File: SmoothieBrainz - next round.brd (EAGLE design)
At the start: 101 x 101 mm, 238 parts, among them IC1 LPC1769, IC7 74LVC1G04, Q1 BSL207SP, Q2 12MHz, SW1 SW_TACT_4P_B, SW3 SW_TACT_4P_B, T1 BC817, U3 USD-SOCKETUSD, X1 MSTBA2, X14 USBPTH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

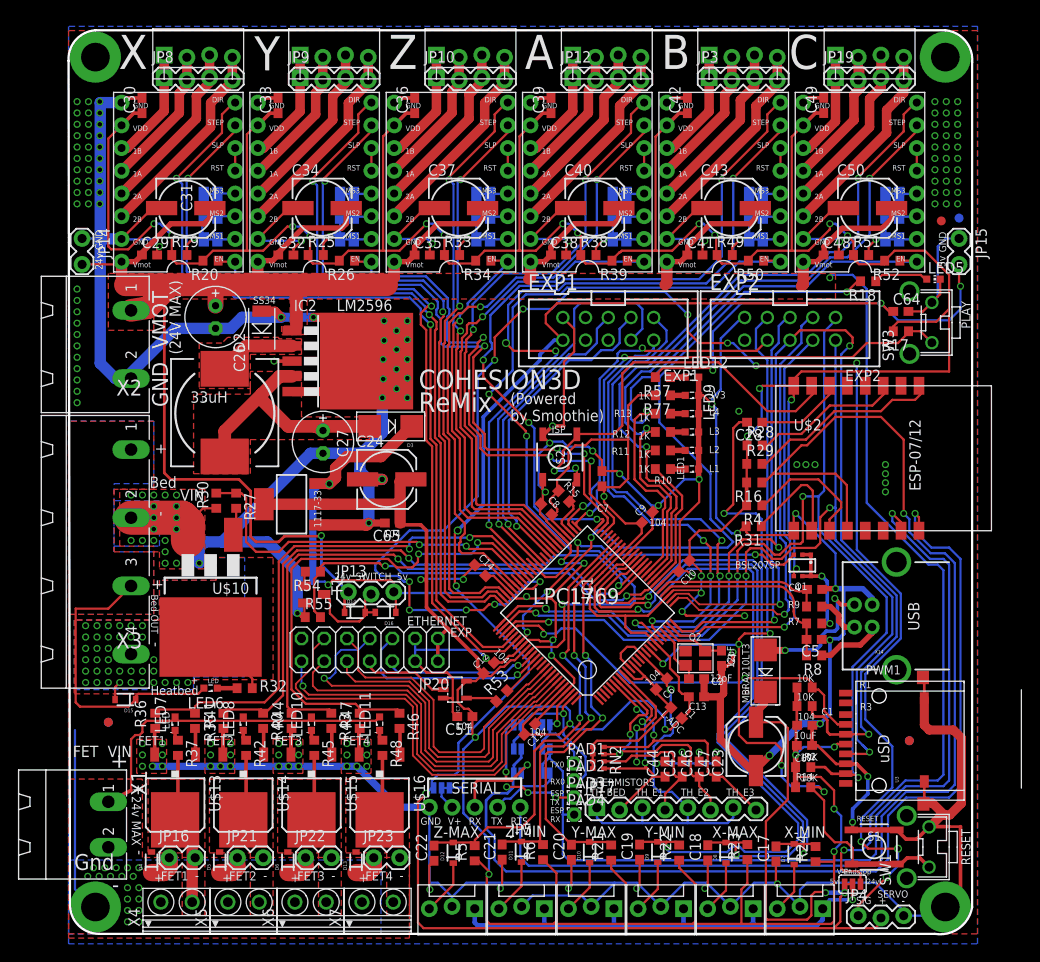
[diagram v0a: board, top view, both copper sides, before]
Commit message: Major routing cleanup per feedback from real engineer
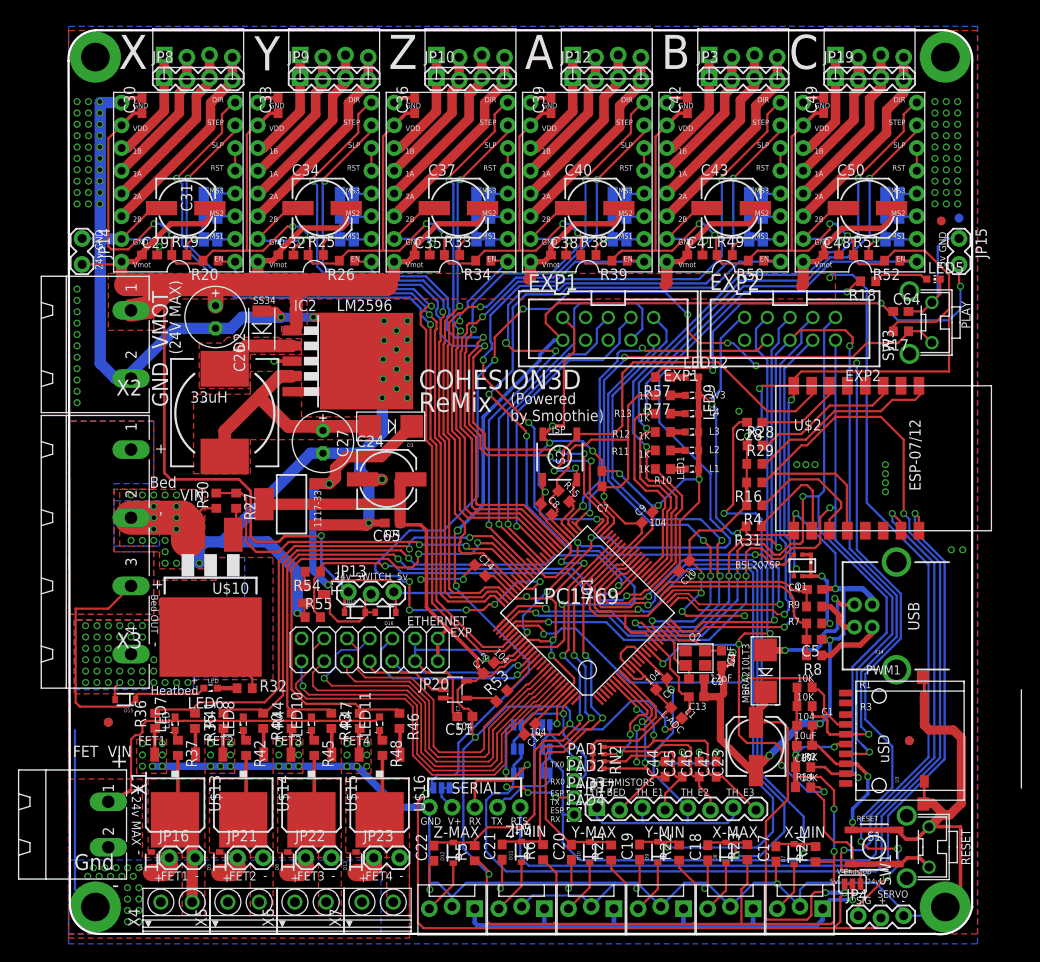
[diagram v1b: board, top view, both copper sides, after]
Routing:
- net Y_MIN: track 86.2 -> 77.3 mm
- net X_MAX: track 78.7 -> 71.8 mm
- net ESPRX: track 101.1 -> 95.6 mm
- net ESPTX: track 119.4 -> 113.9 mm
- net LED4: track 69.4 -> 64.1 mm
- net RTS: track 136.8 -> 131.8 mm
- net 24V: track 318.6 -> 314.5 mm
- net X_MIN: track 70.3 -> 66.8 mm
- net LED3: track 77.0 -> 73.6 mm
- net LED2: track 79.2 -> 76.7 mm
- net DIR1: track 95.0 -> 93.2 mm
- net STP1: track 87.4 -> 85.6 mm
- net EN2: track 58.4 -> 56.9 mm
- net BUZZER-RRD: track 59.1 -> 57.7 mm
- net P1_30_CLICK-ON-RRD: track 49.6 -> 48.2 mm
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
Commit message: About to fix ethernet
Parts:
- C1, C11, C12, C51, C6, C65: value .1uF -> 104
- D2: value (none) -> SS34
- IC2: value (none) -> LM2596-5
- LED1, LED2, LED3, LED4, LED9: value (none) -> GREEN
- LED10, LED11, LED8: value LED -> RED
- LED12: value VMOT -> RED
- LED5: value (none) -> GREEN; device led:CHIP-LED0603 -> led:SML0603
- LED6, LED7: value (none) -> RED
- R10, R11, R12, R13, R77: value (none) -> 1k
- R57: value 1.5k -> 1.5K
- U1: value (none) -> 1117-3.3
- moved XMN 0.79 mm to (83.5, 2.94)
- moved XMX 0.64 mm to (75.9, 2.94)
- moved YMN 0.48 mm to (68.3, 2.94)
- moved C2 0.47 mm to (70.5, 28.1)
- moved C13 0.47 mm to (70.5, 26.1)
- moved YMX 0.32 mm to (60.6, 2.94)
- moved ZMN 0.16 mm to (53.0, 2.94)
- turned LED5 to 180 degrees
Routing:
- net 5V: track 285.2 -> 286.2 mm
- net 3.3V: track 680.7 -> 679.9 mm
- net GND: track 815.3 -> 814.6 mm, vias 189 -> 204
- net PWM1_BED_HEATER: track 42.2 -> 41.6 mm
- net N$1: track 6.45 -> 6.96 mm
